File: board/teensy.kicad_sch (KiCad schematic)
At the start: 1 part, among them U2 Teensy4.1_DEV-16771

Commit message: Redesigning Layout
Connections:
- net DE is gone; now on net AFWhiteLED: U2.14 (A0)
- net AFWhiteLED: no longer U2.31 (CTX3)
- net GantryLED: now also U2.21 (A7); no longer U2.23 (A9)
- net RXD1: now also U2.23 (A9); no longer U2.0 (RX1)
- net RXD2: now also U2.0 (RX1); no longer U2.21 (A7)
- net STBY1: now also U2.19 (A5); no longer U2.3 (LRCLK2)
- net STBY2: now also U2.3 (LRCLK2); no longer U2.19 (A5)
- net TXD1: now also U2.22 (A8); no longer U2.1 (TX1)
- net TXD2: now also U2.1 (TX1); no longer U2.20 (A6)
- net VescLED: now also U2.20 (A6); no longer U2.22 (A8)
- net AFSpareLED renamed SpareLED1
- net AFSparePWM renamed SparePWM1
- net AFSpareSW renamed SpareSW1
- net CacheSpareLED renamed SpareLED2
- net DI: no longer names the net of U2.15 (A1)
- net RE: no longer names the net of U2.13 (SCK)
- net RO: no longer names the net of U2.41 (A17)
- net SCacheSpareSW renamed SpareSW2
- net SoilCacheSparePWM renamed SparePWM2
- net SpareMotorLED renamed Spare12VLED
- no-connect marks 9 -> 13

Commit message: Temporary Designed Layout for review
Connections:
- net AFFLED: now also U2.35 (TX8); no longer U2.11 (MOSI)
- net AFLED365: now also U2.39 (A15); no longer U2.8 (TX2)
- net AFLED405: now also U2.40 (A16); no longer U2.9 (OUT1C)
- net AFLED490: now also U2.41 (A17); no longer U2.10 (CS1)
- net AFLensPWM: now also U2.37 (CS3); no longer U2.12 (MISO)
- net AFLensSW: now also U2.11 (MOSI); no longer U2.39 (A15)
- net AFWhiteLED: now also U2.38 (A14); no longer U2.14 (A0)
- net AugerSW: now also U2.8 (TX2); no longer U2.40 (A16)
- net Dir_Switch: now also U2.29 (TX7); no longer U2.33 (MCLK2)
- net GantryLED: now also U2.30 (CRX3); no longer U2.21 (A7)
- net GantrySW: now also U2.12 (MISO); no longer U2.18 (A4)
- net GimbalPanLED: now also U2.36 (CS2); no longer U2.25 (A11)
- net GimbalPanSW: now also U2.10 (CS1); no longer U2.37 (CS3)
- net GimbalTiltLED: now also U2.20 (A6); no longer U2.7 (RX2)
- net GimbalTiltSW: now also U2.6 (OUT1D); no longer U2.34 (RX8)
- net Moisture: now also U2.24 (A10); no longer U2.27 (A13)
- net STBY1: now also U2.27 (A13); no longer U2.19 (A5)
- net STBY2: now also U2.28 (RX7); no longer U2.3 (LRCLK2)
- net SciGimbalPan: now also U2.13 (SCK); no longer U2.24 (A10)
- net SciGimbalTilt: now also U2.19 (A5); no longer U2.6 (OUT1D)
- net SoilDoorSW: now also U2.7 (RX2); no longer U2.17 (A3)
- net SoilTDLED: now also U2.17 (A3); no longer U2.4 (BCLK2)
- net SoilTrapdoorPWM: now also U2.15 (A1); no longer U2.5 (IN2)
- net Spare12VLED: now also U2.33 (MCLK2); no longer U2.2 (OUT2)
- net SpareLED1: now also U2.16 (A2); no longer U2.30 (CRX3)
- net SpareLED2: now also U2.21 (A7); no longer U2.26 (A12)
- net SparePWM1: now also U2.14 (A0); no longer U2.29 (TX7)
- net SparePWM2: now also U2.18 (A4); no longer U2.28 (RX7)
- net SpareSW1: now also U2.9 (OUT1C); no longer U2.35 (TX8)
- net SpareSW2: now also U2.5 (IN2); no longer U2.16 (A2)
- net SpareSW_12V: now also U2.26 (A12); no longer U2.36 (CS2)
- net Temp: now also U2.25 (A11); no longer U2.38 (A14)
- net VescLED: now also U2.34 (RX8); no longer U2.20 (A6)

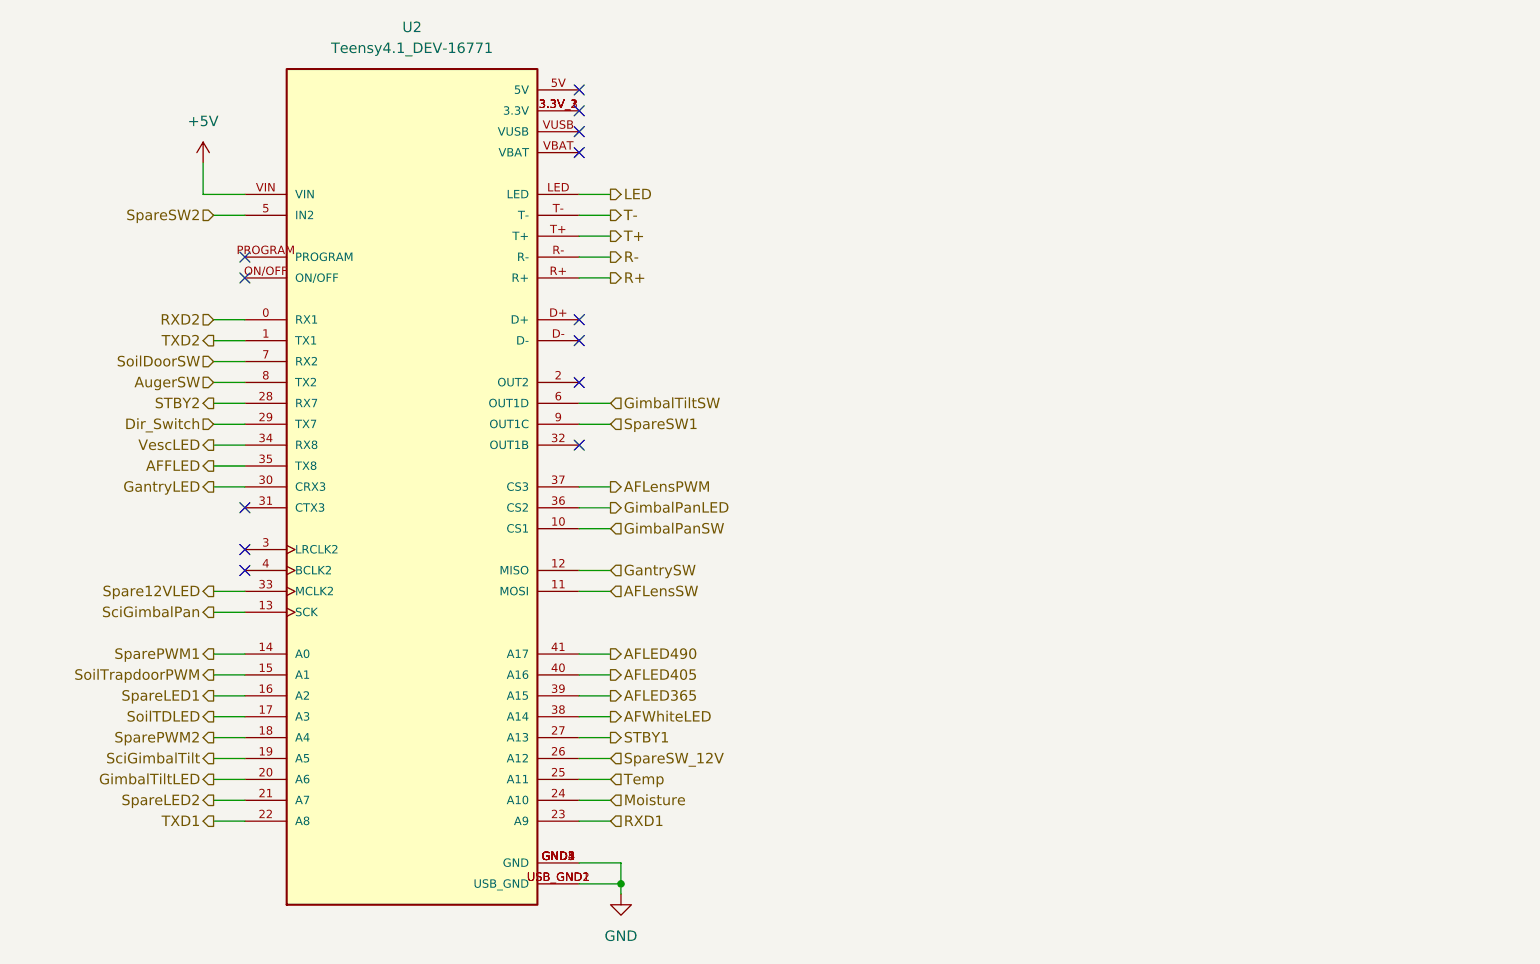
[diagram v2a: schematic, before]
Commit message: updated teensy pinout
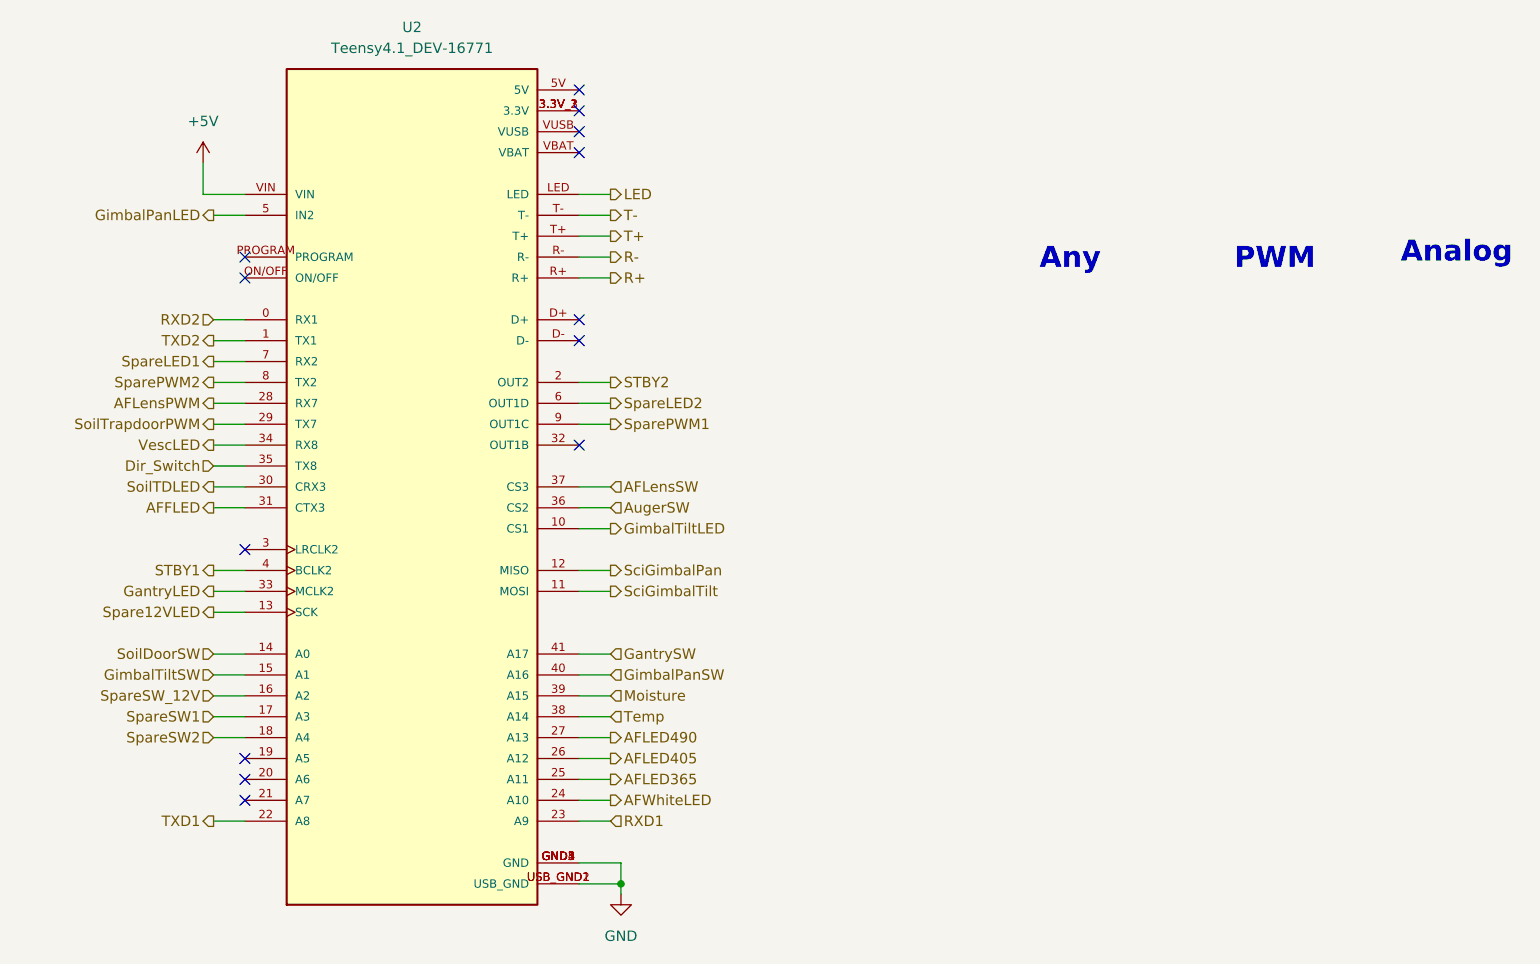
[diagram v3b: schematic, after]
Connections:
- net AFFLED: now also U2.31 (CTX3); no longer U2.35 (TX8)
- net AFLED365: now also U2.25 (A11); no longer U2.39 (A15)
- net AFLED405: now also U2.26 (A12); no longer U2.40 (A16)
- net AFLED490: now also U2.27 (A13); no longer U2.41 (A17)
- net AFLensPWM: now also U2.28 (RX7); no longer U2.37 (CS3)
- net AFLensSW: now also U2.37 (CS3); no longer U2.11 (MOSI)
- net AFWhiteLED: now also U2.24 (A10); no longer U2.38 (A14)
- net AugerSW: now also U2.36 (CS2); no longer U2.8 (TX2)
- net Dir_Switch: now also U2.35 (TX8); no longer U2.29 (TX7)
- net GantryLED: now also U2.33 (MCLK2); no longer U2.30 (CRX3)
- net GantrySW: now also U2.41 (A17); no longer U2.12 (MISO)
- net GimbalPanLED: now also U2.5 (IN2); no longer U2.36 (CS2)
- net GimbalPanSW: now also U2.40 (A16); no longer U2.10 (CS1)
- net GimbalTiltLED: now also U2.10 (CS1); no longer U2.20 (A6)
- net GimbalTiltSW: now also U2.15 (A1); no longer U2.6 (OUT1D)
- net Moisture: now also U2.39 (A15); no longer U2.24 (A10)
- net STBY1: now also U2.4 (BCLK2); no longer U2.27 (A13)
- net STBY2: now also U2.2 (OUT2); no longer U2.28 (RX7)
- net SciGimbalPan: now also U2.12 (MISO); no longer U2.13 (SCK)
- net SciGimbalTilt: now also U2.11 (MOSI); no longer U2.19 (A5)
- net SoilDoorSW: now also U2.14 (A0); no longer U2.7 (RX2)
- net SoilTDLED: now also U2.30 (CRX3); no longer U2.17 (A3)
- net SoilTrapdoorPWM: now also U2.29 (TX7); no longer U2.15 (A1)
- net Spare12VLED: now also U2.13 (SCK); no longer U2.33 (MCLK2)
- net SpareLED1: now also U2.7 (RX2); no longer U2.16 (A2)
- net SpareLED2: now also U2.6 (OUT1D); no longer U2.21 (A7)
- net SparePWM1: now also U2.9 (OUT1C); no longer U2.14 (A0)
- net SparePWM2: now also U2.8 (TX2); no longer U2.18 (A4)
- net SpareSW1: now also U2.17 (A3); no longer U2.9 (OUT1C)
- net SpareSW2: now also U2.18 (A4); no longer U2.5 (IN2)
- net SpareSW_12V: now also U2.16 (A2); no longer U2.26 (A12)
- net Temp: now also U2.38 (A14); no longer U2.25 (A11)
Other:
- note added: "Analog"
- note added: "Any"
- note added: "PWM"

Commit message: preliminary routing
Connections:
- net Moisture: now also U2.38 (A14); no longer U2.39 (A15)
- net Temp: now also U2.39 (A15); no longer U2.38 (A14)

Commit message: added changes from board review
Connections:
- net AFLED405: now also U2.19 (A5); no longer U2.26 (A12)
- net AFLED490: now also U2.3 (LRCLK2); no longer U2.27 (A13)
- net Moisture: now also U2.27 (A13); no longer U2.38 (A14)
- net Temp: now also U2.26 (A12); no longer U2.39 (A15)

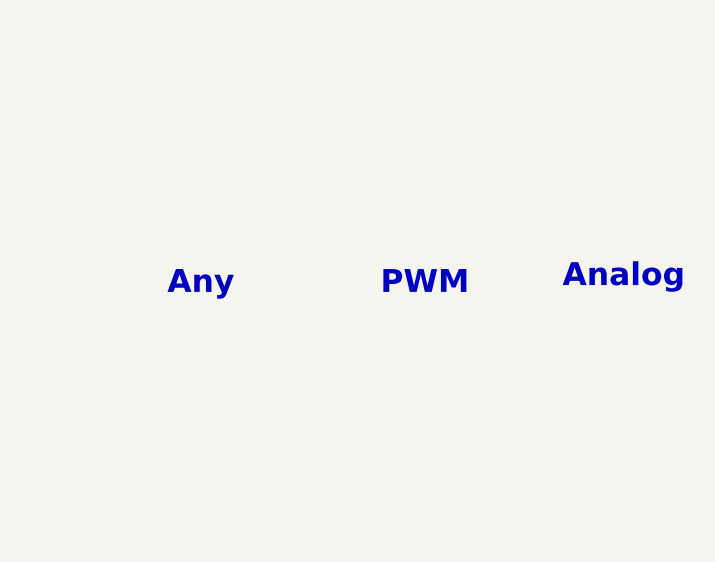
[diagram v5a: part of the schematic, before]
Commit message: updated based on overlord jesse's input
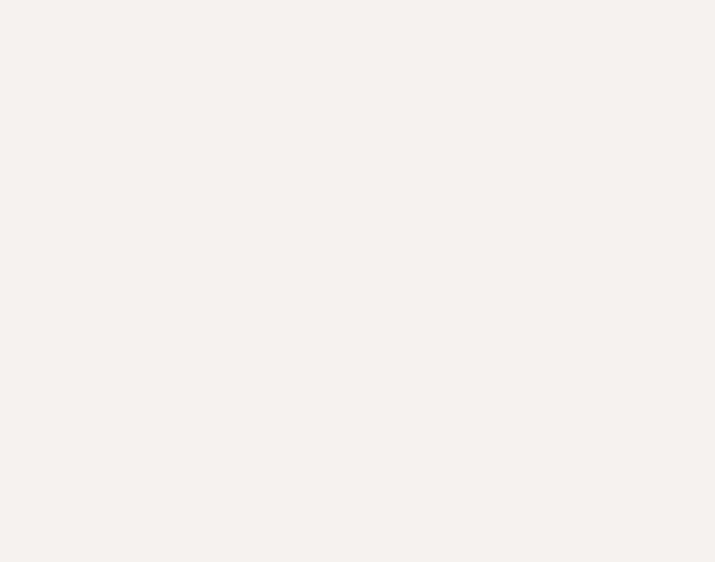
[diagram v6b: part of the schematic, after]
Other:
- note removed: "Analog"
- note removed: "Any"
- note removed: "PWM"
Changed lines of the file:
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@@
 	(generator_version "9.0")
 	(paper "A4")
-	(text "Analog\n"
-		(exclude_from_sim no)
-		(at 271.78 60.452 0)
-		(effects
-			(font
-				(size 2.54 2.54)
-				(thickness 0.508)
-				(bold yes)
-			)
-		)
-	)
-	(text "PWM"
-		(exclude_from_sim no)
-		(at 249.682 61.214 0)
-		(effects
-			(font
-				(size 2.54 2.54)
-				(thickness 0.508)
-				(bold yes)
-			)
-		)
-	)
-	(text "Any"
-		(exclude_from_sim no)
-		(at 224.79 61.214 0)
-		(effects
-			(font
-				(size 2.54 2.54)
-				(thickness 0.508)
-				(bold yes)
-			)
-		)
-	)
 	(junction
 		(at 170.18 137.16)
